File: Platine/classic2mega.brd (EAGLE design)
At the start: 57.5 x 44.5 mm, 26 parts, among them IC2 74HC157N, IC3 MEGA8-P, U1 MCP1700_SOT23, U2 BSS138_SOT23, U3 BSS138_SOT23

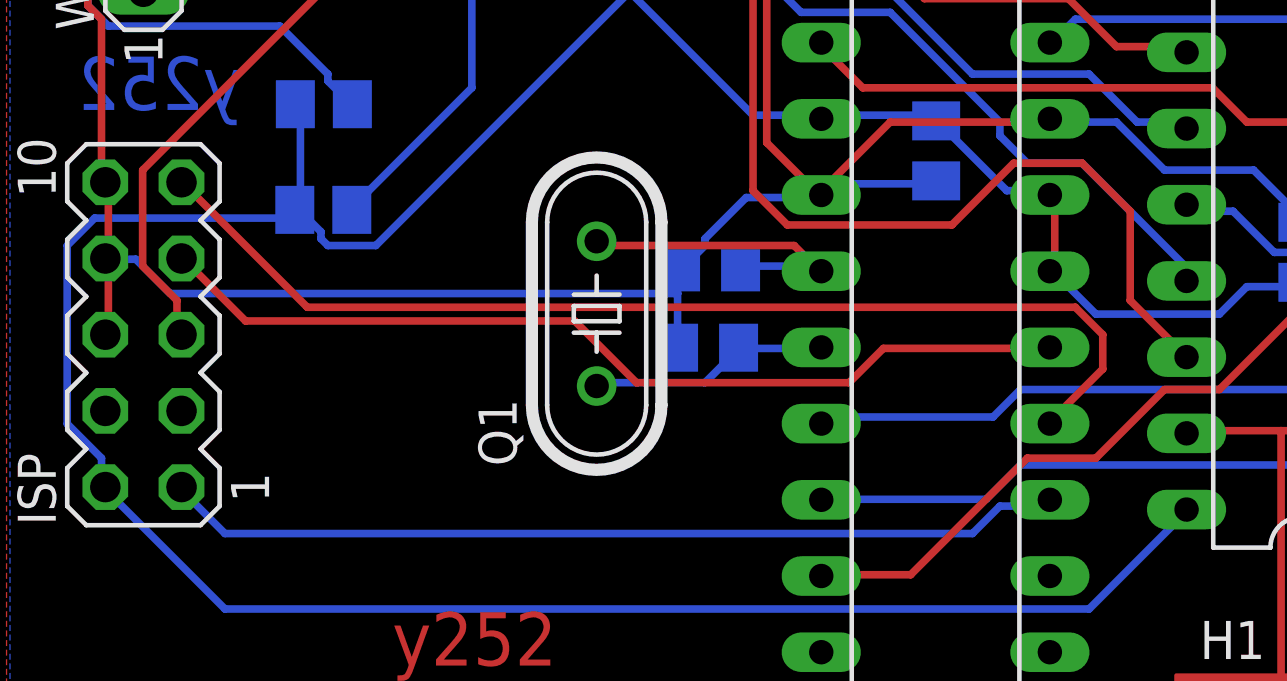
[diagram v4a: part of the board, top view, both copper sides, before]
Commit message: Remove signal lines under crystal
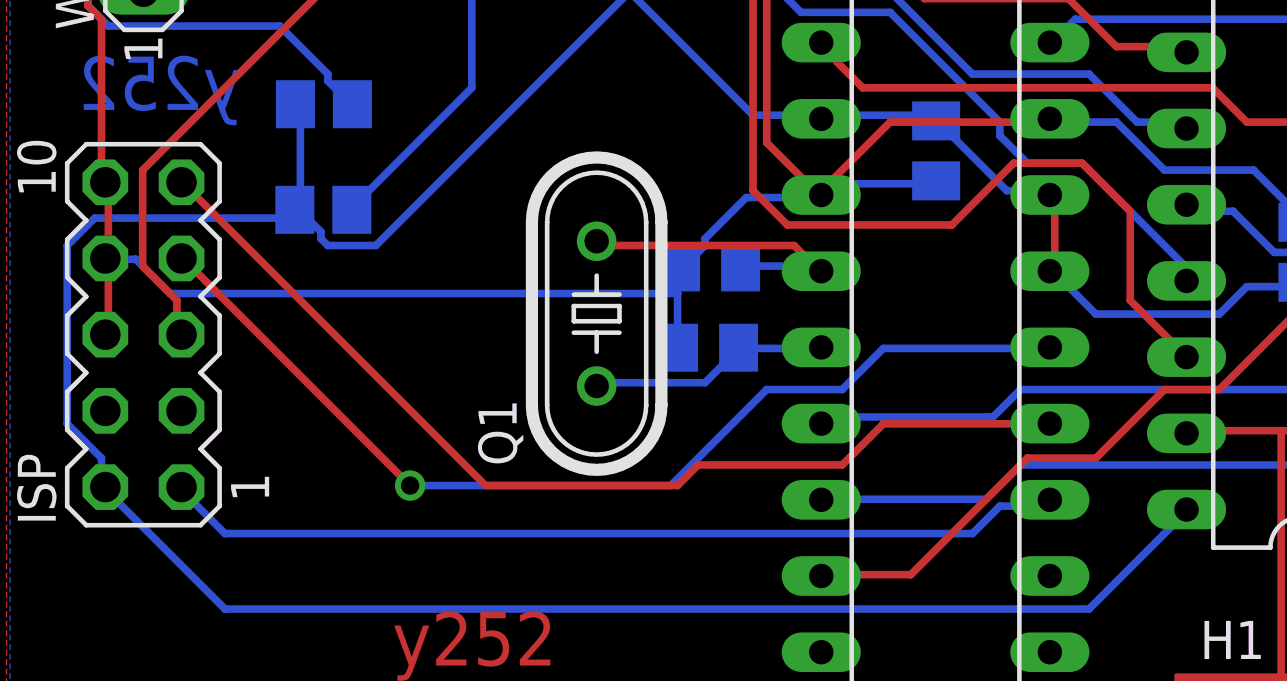
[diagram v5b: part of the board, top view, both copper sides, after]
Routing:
- net SCK: track 31.1 -> 34.0 mm, vias 0 -> 1
- net MISO: track 36.5 -> 34.3 mm
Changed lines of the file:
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@@
 <layers>
 <layer number="1" name="Top" color="4" fill="1" visible="yes" active="yes"/>
-<layer number="16" name="Bottom" color="1" fill="1" visible="no" active="yes"/>
+<layer number="16" name="Bottom" color="1" fill="1" visible="yes" active="yes"/>
 <layer number="17" name="Pads" color="2" fill="1" visible="yes" active="yes"/>
 <layer number="18" name="Vias" color="2" fill="1" visible="yes" active="yes"/>
@@
 <layer number="40" name="bKeepout" color="1" fill="11" visible="no" active="yes"/>
 <layer number="41" name="tRestrict" color="4" fill="10" visible="yes" active="yes"/>
-<layer number="42" name="bRestrict" color="1" fill="10" visible="no" active="yes"/>
+<layer number="42" name="bRestrict" color="1" fill="10" visible="yes" active="yes"/>
 <layer number="43" name="vRestrict" color="2" fill="10" visible="no" active="yes"/>
 <layer number="44" name="Drills" color="7" fill="1" visible="no" active="yes"/>
@@
 <element name="U$6" library="case_holes" package="G028-HOLES" value="" x="15.245190625" y="62.230759375"/>
 <element name="U3" library="BSS138" package="SOT23" value="BSS138_SOT23" x="35.4326625" y="51.40220625" smashed="yes" rot="MR90">
-<attribute name="NAME" x="34.818359375" y="53.191590625" size="1.27" layer="26" rot="MR90"/>
+<attribute name="NAME" x="32.158121875" y="50.06611875" size="1.27" layer="26" rot="MR90"/>
 <attribute name="VALUE" x="32.2576625" y="49.49720625" size="1.27" layer="28" rot="MR90"/>
 </element>
@@
 <contactref element="ISP" pad="9"/>
 <contactref element="IC3" pad="18"/>
-<wire x1="57.3786" y1="33.147" x2="55.7784" y2="31.5468" width="0.254" layer="1"/>
-<wire x1="57.3786" y1="34.29" x2="57.3786" y2="33.147" width="0.254" layer="1"/>
-<wire x1="56.4642" y1="35.2044" x2="57.3786" y2="34.29" width="0.254" layer="1"/>
-<wire x1="30.861" y1="35.2044" x2="56.4642" y2="35.2044" width="0.254" layer="1"/>
-<wire x1="26.7462" y1="39.3192" x2="30.861" y2="35.2044" width="0.254" layer="1"/>
 <wire x1="55.7784" y1="31.5468" x2="55.61455625" y2="31.3258" width="0.254" layer="1"/>
+<wire x1="50.0634" y1="31.3182" x2="55.5498" y2="31.3182" width="0.254" layer="1"/>
+<wire x1="48.6918" y1="29.9466" x2="50.0634" y2="31.3182" width="0.254" layer="1"/>
+<wire x1="43.8912" y1="29.9466" x2="48.6918" y2="29.9466" width="0.254" layer="1"/>
+<wire x1="43.2054" y1="29.2608" x2="43.8912" y2="29.9466" width="0.254" layer="1"/>
+<wire x1="36.8046" y1="29.2608" x2="43.2054" y2="29.2608" width="0.254" layer="1"/>
+<wire x1="26.7462" y1="39.3192" x2="36.8046" y2="29.2608" width="0.254" layer="1"/>
+<wire x1="55.5498" y1="31.3182" x2="55.61455625" y2="31.3258" width="0.254" layer="1"/>
 <wire x1="26.7462" y1="39.3192" x2="26.67" y2="39.37" width="0.254" layer="1"/>
 </signal>
@@
 <contactref element="ISP" pad="7"/>
 <contactref element="IC3" pad="19"/>
-<wire x1="50.0634" y1="33.8328" x2="55.5498" y2="33.8328" width="0.254" layer="1"/>
-<wire x1="48.9204" y1="32.6898" x2="50.0634" y2="33.8328" width="0.254" layer="1"/>
-<wire x1="41.8338" y1="32.6898" x2="48.9204" y2="32.6898" width="0.254" layer="1"/>
-<wire x1="39.7764" y1="34.7472" x2="41.8338" y2="32.6898" width="0.254" layer="1"/>
-<wire x1="28.8036" y1="34.7472" x2="39.7764" y2="34.7472" width="0.254" layer="1"/>
-<wire x1="26.7462" y1="36.8046" x2="28.8036" y2="34.7472" width="0.254" layer="1"/>
 <wire x1="55.5498" y1="33.8328" x2="55.61455625" y2="33.8658" width="0.254" layer="1"/>
+<wire x1="50.0634" y1="33.8328" x2="55.5498" y2="33.8328" width="0.254" layer="16"/>
+<wire x1="48.6918" y1="32.4612" x2="50.0634" y2="33.8328" width="0.254" layer="16"/>
+<wire x1="46.1772" y1="32.4612" x2="48.6918" y2="32.4612" width="0.254" layer="16"/>
+<wire x1="42.9768" y1="29.2608" x2="46.1772" y2="32.4612" width="0.254" layer="16"/>
+<wire x1="34.29" y1="29.2608" x2="42.9768" y2="29.2608" width="0.254" layer="16"/>
+<wire x1="26.7462" y1="36.8046" x2="34.29" y2="29.2608" width="0.254" layer="1"/>
+<wire x1="55.5498" y1="33.8328" x2="55.61455625" y2="33.8658" width="0.254" layer="16"/>
 <wire x1="26.7462" y1="36.8046" x2="26.67" y2="36.83" width="0.254" layer="1"/>
+<via x="34.29" y="29.2608" extent="1-16" drill="0.6096"/>
 </signal>
 <signal name="3.3V">

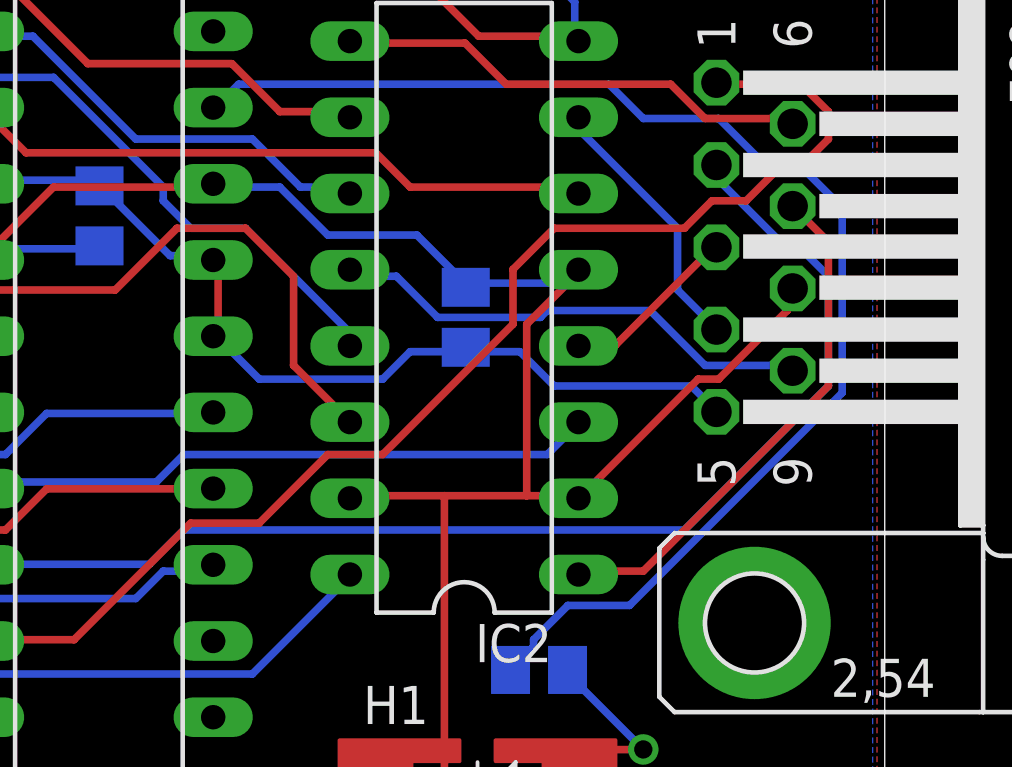
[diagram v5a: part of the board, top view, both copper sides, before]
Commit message: Move 100nf closer to 5v of ic
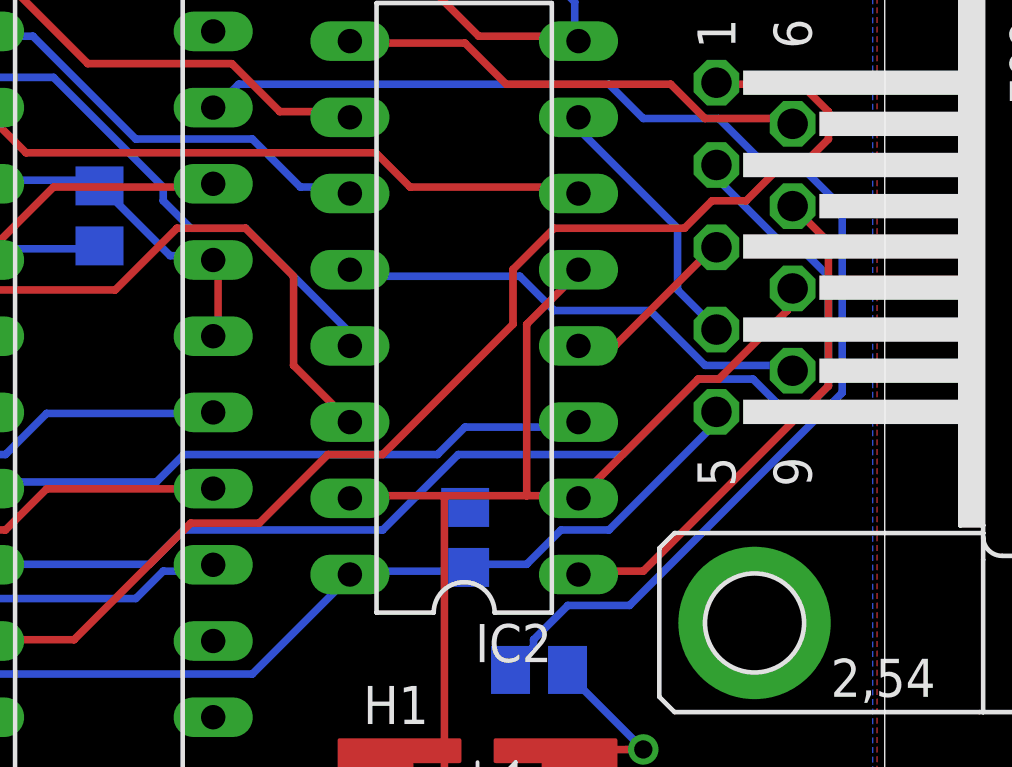
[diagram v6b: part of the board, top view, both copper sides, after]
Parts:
- moved C7 7.34 mm to (64.0, 29.7)
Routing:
- net GND: track 188.2 -> 174.3 mm
- net 5V: track 136.8 -> 132.8 mm
- net PAD_DOWN: track 39.8 -> 40.5 mm
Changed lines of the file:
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@@
 <layers>
 <layer number="1" name="Top" color="4" fill="1" visible="yes" active="yes"/>
-<layer number="16" name="Bottom" color="1" fill="1" visible="yes" active="yes"/>
+<layer number="16" name="Bottom" color="1" fill="1" visible="no" active="yes"/>
 <layer number="17" name="Pads" color="2" fill="1" visible="yes" active="yes"/>
 <layer number="18" name="Vias" color="2" fill="1" visible="yes" active="yes"/>
@@
 <layer number="40" name="bKeepout" color="1" fill="11" visible="no" active="yes"/>
 <layer number="41" name="tRestrict" color="4" fill="10" visible="yes" active="yes"/>
-<layer number="42" name="bRestrict" color="1" fill="10" visible="yes" active="yes"/>
+<layer number="42" name="bRestrict" color="1" fill="10" visible="no" active="yes"/>
 <layer number="43" name="vRestrict" color="2" fill="10" visible="no" active="yes"/>
 <layer number="44" name="Drills" color="7" fill="1" visible="no" active="yes"/>
@@
 </element>
 <element name="IC2" library="74xx-eu" library_urn="urn:adsk.eagle:library:85" package="DIL16" package3d_urn="urn:adsk.eagle:package:2009/1" value="74HC157N" x="63.9812125" y="37.352121875" rot="R90"/>
-<element name="C7" library="resistor" package="C0805K" value="100n" x="64.032396875" y="37.035734375" smashed="yes" rot="MR270">
-<attribute name="NAME" x="62.927065625" y="37.889178125" size="1.016" layer="26" rot="MR270"/>
-<attribute name="VALUE" x="65.932396875" y="38.035734375" size="1.016" layer="28" rot="MR270"/>
+<element name="C7" library="resistor" package="C0805K" value="100n" x="64.0122125" y="29.697996875" smashed="yes" rot="MR270">
+<attribute name="NAME" x="62.90688125" y="30.551440625" size="1.016" layer="26" rot="MR270"/>
+<attribute name="VALUE" x="65.9122125" y="30.697996875" size="1.016" layer="28" rot="MR270"/>
 </element>
 <element name="R7" library="resistor" package="M0805" value="1M" x="63.679828125" y="56.541690625" rot="MR0"/>
@@
 <wire x1="55.5498" y1="41.3766" x2="55.61455625" y2="41.4858" width="0.254" layer="1"/>
 <wire x1="48.006" y1="39.0906" x2="47.99455625" y2="38.9458" width="0.254" layer="1"/>
-<wire x1="67.437" y1="38.1762" x2="64.2366" y2="38.1762" width="0.254" layer="16"/>
-<wire x1="67.6656" y1="38.4048" x2="67.437" y2="38.1762" width="0.254" layer="16"/>
-<wire x1="64.2366" y1="38.1762" x2="64.032396875" y2="38.035734375" width="0.254" layer="16"/>
-<wire x1="67.6656" y1="38.4048" x2="67.7912125" y2="38.622121875" width="0.254" layer="16"/>
 <wire x1="67.6656" y1="31.0896" x2="66.0654" y2="31.0896" width="0.254" layer="1"/>
 <wire x1="66.0654" y1="31.0896" x2="63.3222" y2="31.0896" width="0.254" layer="1"/>
@@
 <wire x1="66.0654" y1="31.0896" x2="66.0654" y2="36.8046" width="0.254" layer="1"/>
 <wire x1="67.6656" y1="38.4048" x2="67.7912125" y2="38.622121875" width="0.254" layer="1"/>
-<wire x1="57.8358" y1="41.3766" x2="55.7784" y2="41.3766" width="0.254" layer="16"/>
-<wire x1="59.436" y1="39.7764" x2="57.8358" y2="41.3766" width="0.254" layer="16"/>
-<wire x1="62.4078" y1="39.7764" x2="59.436" y2="39.7764" width="0.254" layer="16"/>
-<wire x1="64.008" y1="38.1762" x2="62.4078" y2="39.7764" width="0.254" layer="16"/>
-<wire x1="55.7784" y1="41.3766" x2="55.61455625" y2="41.4858" width="0.254" layer="16"/>
-<wire x1="64.008" y1="38.1762" x2="64.032396875" y2="38.035734375" width="0.254" layer="16"/>
 <wire x1="25.146" y1="36.8046" x2="24.2316" y2="36.8046" width="0.254" layer="16"/>
 <wire x1="26.289" y1="35.6616" x2="25.146" y2="36.8046" width="0.254" layer="16"/>
@@
 <wire x1="60.1218" y1="28.3464" x2="60.1712125" y2="28.462121875" width="0.254" layer="16"/>
 <wire x1="24.2316" y1="29.0322" x2="24.13" y2="29.21" width="0.254" layer="16"/>
-<wire x1="65.8368" y1="35.8902" x2="64.2366" y2="35.8902" width="0.254" layer="16"/>
-<wire x1="66.9798" y1="34.7472" x2="65.8368" y2="35.8902" width="0.254" layer="16"/>
-<wire x1="71.5518" y1="34.7472" x2="66.9798" y2="34.7472" width="0.254" layer="16"/>
-<wire x1="72.2376" y1="34.0614" x2="71.5518" y2="34.7472" width="0.254" layer="16"/>
-<wire x1="64.2366" y1="35.8902" x2="64.032396875" y2="36.035734375" width="0.254" layer="16"/>
-<wire x1="72.2376" y1="34.0614" x2="72.39" y2="33.8836" width="0.254" layer="16"/>
 <wire x1="42.7482" y1="59.6646" x2="40.4622" y2="59.6646" width="0.254" layer="16"/>
 <wire x1="40.4622" y1="59.6646" x2="39.3192" y2="59.6646" width="0.254" layer="16"/>
@@
 <wire x1="40.4622" y1="47.0916" x2="40.4622" y2="48.6918" width="0.254" layer="16"/>
 <wire x1="40.4622" y1="47.0916" x2="40.34860625" y2="47.0610625" width="0.254" layer="16"/>
-<wire x1="62.1792" y1="35.8902" x2="64.008" y2="35.8902" width="0.254" layer="16"/>
-<wire x1="61.2648" y1="34.9758" x2="62.1792" y2="35.8902" width="0.254" layer="16"/>
-<wire x1="57.15" y1="34.9758" x2="61.2648" y2="34.9758" width="0.254" layer="16"/>
-<wire x1="55.7784" y1="36.3474" x2="57.15" y2="34.9758" width="0.254" layer="16"/>
-<wire x1="64.008" y1="35.8902" x2="64.032396875" y2="36.035734375" width="0.254" layer="16"/>
-<wire x1="55.7784" y1="36.3474" x2="55.61455625" y2="36.4058" width="0.254" layer="16"/>
 <wire x1="24.003" y1="30.1752" x2="24.003" y2="29.2608" width="0.254" layer="16"/>
 <wire x1="22.86" y1="31.3182" x2="24.003" y2="30.1752" width="0.254" layer="16"/>
@@
 <wire x1="34.5186" y1="58.9788" x2="34.4975625" y2="58.816825" width="0.254" layer="16"/>
 <wire x1="39.0906" y1="59.436" x2="39.102178125" y2="59.64065625" width="0.254" layer="16"/>
+<wire x1="60.3504" y1="28.575" x2="64.008" y2="28.575" width="0.254" layer="16"/>
+<wire x1="64.008" y1="28.575" x2="64.0122125" y2="28.697996875" width="0.254" layer="16"/>
+<wire x1="60.3504" y1="28.575" x2="60.1712125" y2="28.462121875" width="0.254" layer="16"/>
+<wire x1="66.0654" y1="28.8036" x2="64.2366" y2="28.8036" width="0.254" layer="16"/>
+<wire x1="67.2084" y1="29.9466" x2="66.0654" y2="28.8036" width="0.254" layer="16"/>
+<wire x1="68.8086" y1="29.9466" x2="67.2084" y2="29.9466" width="0.254" layer="16"/>
+<wire x1="72.2376" y1="33.3756" x2="68.8086" y2="29.9466" width="0.254" layer="16"/>
+<wire x1="72.2376" y1="33.8328" x2="72.2376" y2="33.3756" width="0.254" layer="16"/>
+<wire x1="64.2366" y1="28.8036" x2="64.0122125" y2="28.697996875" width="0.254" layer="16"/>
+<wire x1="72.2376" y1="33.8328" x2="72.39" y2="33.8836" width="0.254" layer="16"/>
 </signal>
 <signal name="RESET">
@@
 <wire x1="53.4924" y1="28.8036" x2="48.006" y2="28.8036" width="0.254" layer="16"/>
 <wire x1="54.6354" y1="29.9466" x2="53.4924" y2="28.8036" width="0.254" layer="16"/>
-<wire x1="71.3232" y1="29.9466" x2="54.6354" y2="29.9466" width="0.254" layer="16"/>
-<wire x1="76.1238" y1="34.7472" x2="71.3232" y2="29.9466" width="0.254" layer="16"/>
+<wire x1="61.2648" y1="29.9466" x2="54.6354" y2="29.9466" width="0.254" layer="16"/>
+<wire x1="63.7794" y1="32.4612" x2="61.2648" y2="29.9466" width="0.254" layer="16"/>
+<wire x1="69.2658" y1="32.4612" x2="63.7794" y2="32.4612" width="0.254" layer="16"/>
+<wire x1="71.7804" y1="34.9758" x2="69.2658" y2="32.4612" width="0.254" layer="16"/>
+<wire x1="73.6092" y1="34.9758" x2="71.7804" y2="34.9758" width="0.254" layer="16"/>
+<wire x1="74.5236" y1="34.0614" x2="73.6092" y2="34.9758" width="0.254" layer="16"/>
+<wire x1="75.438" y1="34.0614" x2="74.5236" y2="34.0614" width="0.254" layer="16"/>
+<wire x1="76.1238" y1="34.7472" x2="75.438" y2="34.0614" width="0.254" layer="16"/>
 <wire x1="76.1238" y1="38.4048" x2="76.1238" y2="34.7472" width="0.254" layer="16"/>
 <wire x1="74.9808" y1="39.5478" x2="76.1238" y2="38.4048" width="0.254" layer="16"/>
@@
 <wire x1="53.721" y1="31.5468" x2="48.006" y2="31.5468" width="0.254" layer="16"/>
 <wire x1="54.6354" y1="32.4612" x2="53.721" y2="31.5468" width="0.254" layer="16"/>
-<wire x1="66.7512" y1="32.4612" x2="54.6354" y2="32.4612" width="0.254" layer="16"/>
-<wire x1="67.6656" y1="33.3756" x2="66.7512" y2="32.4612" width="0.254" layer="16"/>
+<wire x1="63.0936" y1="32.4612" x2="54.6354" y2="32.4612" width="0.254" layer="16"/>
+<wire x1="64.008" y1="33.3756" x2="63.0936" y2="32.4612" width="0.254" layer="16"/>
+<wire x1="67.6656" y1="33.3756" x2="64.008" y2="33.3756" width="0.254" layer="16"/>
 <wire x1="48.006" y1="31.5468" x2="47.99455625" y2="31.3258" width="0.254" layer="16"/>
 <wire x1="67.6656" y1="33.3756" x2="67.7912125" y2="33.542121875" width="0.254" layer="16"/>
@@
 <contactref element="IC2" pad="12"/>
 <contactref element="X1" pad="9"/>
-<wire x1="61.722" y1="38.4048" x2="60.3504" y2="38.4048" width="0.254" layer="16"/>
-<wire x1="63.0936" y1="37.0332" x2="61.722" y2="38.4048" width="0.254" layer="16"/>
-<wire x1="66.5226" y1="37.0332" x2="63.0936" y2="37.0332" width="0.254" layer="16"/>
-<wire x1="66.7512" y1="37.2618" x2="66.5226" y2="37.0332" width="0.254" layer="16"/>
-<wire x1="70.1802" y1="37.2618" x2="66.7512" y2="37.2618" width="0.254" layer="16"/>
+<wire x1="65.8368" y1="38.4048" x2="60.3504" y2="38.4048" width="0.254" layer="16"/>
+<wire x1="66.9798" y1="37.2618" x2="65.8368" y2="38.4048" width="0.254" layer="16"/>
+<wire x1="70.1802" y1="37.2618" x2="66.9798" y2="37.2618" width="0.254" layer="16"/>
 <wire x1="72.009" y1="35.433" x2="70.1802" y2="37.2618" width="0.254" layer="16"/>
 <wire x1="74.7522" y1="35.433" x2="72.009" y2="35.433" width="0.254" layer="16"/>
